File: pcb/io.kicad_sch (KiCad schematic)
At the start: 36 parts, among them J10 Conn_01x02, J2 RJ18, J3 RJ18, J4 Conn_02x05, J5 Conn_01x03, J6 Conn_01x03, J7 Conn_01x02, J8 Conn_01x02, J9 Conn_01x02, Q1 BT148, Q2 BC847, Q3 BC847, U7 6N137, U8 PC817, U9 PC817

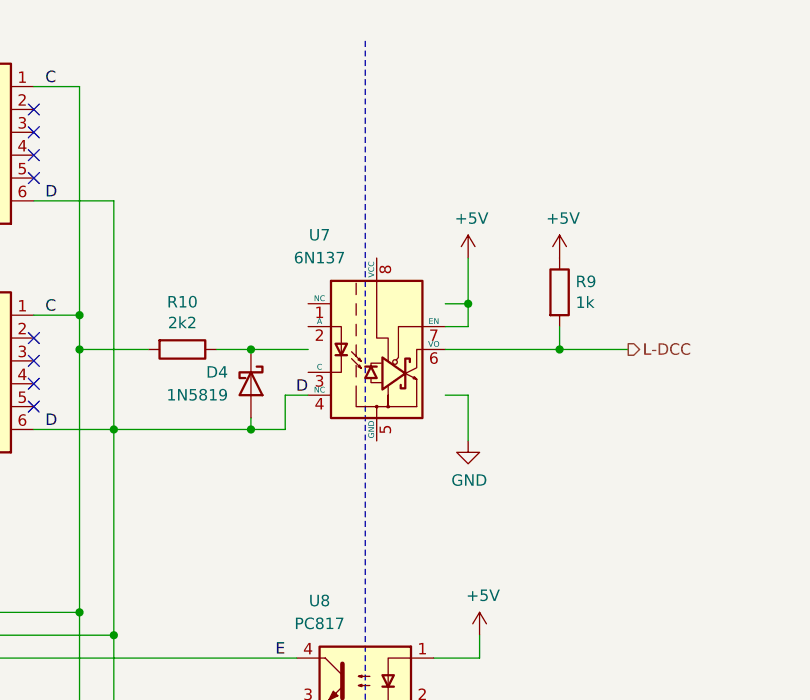
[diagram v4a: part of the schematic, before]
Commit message: Add capacitor to U7, fix new parts.
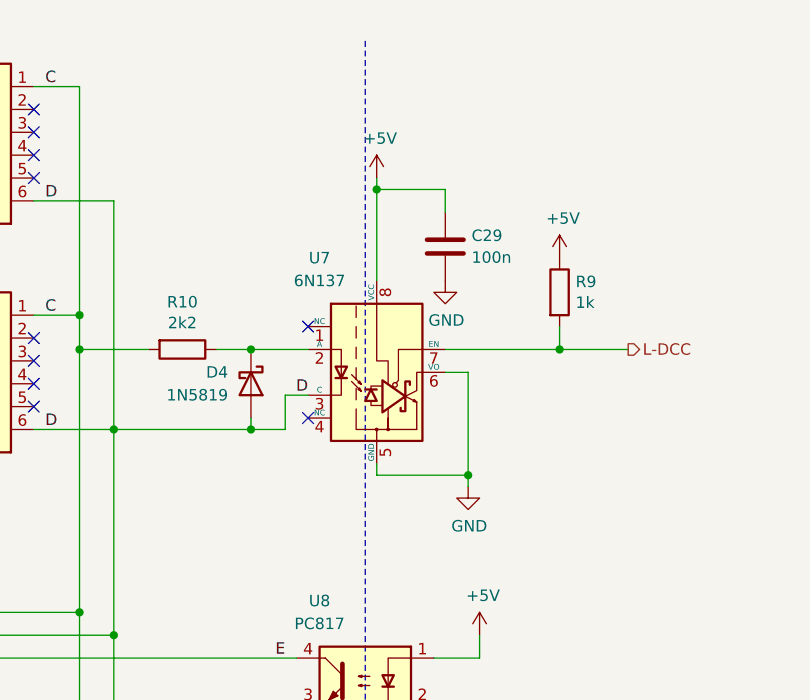
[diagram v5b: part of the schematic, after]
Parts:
- added C29: 100n, Capacitor_SMD:C_0805_2012Metric, symbol Device:C
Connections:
- net +5V: now also U7.8 (VCC), C29.1; no longer U7.7 (EN)
- net D: now also U7.3 (C); no longer U7.4 (NC)
- net GND: now also U7.5 (GND), U7.6 (VO), C29.2
- net L-DCC: now also U7.7 (EN); no longer U7.6 (VO)
- net at U7.2 (A): now also D4.1 (K), R10.1
- no-connect marks 9 -> 11
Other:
- moved on the sheet: U7
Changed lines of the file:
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@@
 	)
 	(junction
+		(at 83.82 35.56)
+		(diameter 0)
+		(color 0 0 0 0)
+	)
+	(junction
 		(at 204.47 55.88)
 		(diameter 0)
@@
 	)
 	(junction
-		(at 93.98 48.26)
+		(at 255.27 123.19)
 		(diameter 0)
 		(color 0 0 0 0)
 	)
 	(junction
-		(at 255.27 123.19)
+		(at 69.85 53.34)
 		(diameter 0)
 		(color 0 0 0 0)
 	)
 	(junction
-		(at 69.85 53.34)
+		(at 214.63 102.87)
 		(diameter 0)
 		(color 0 0 0 0)
 	)
 	(junction
-		(at 214.63 102.87)
+		(at 93.98 67.31)
 		(diameter 0)
 		(color 0 0 0 0)
@@
 	)
 	(no_connect
+		(at 76.2 60.96)
+	)
+	(no_connect
 		(at 45.72 26.67)
 	)
@@
 	)
 	(no_connect
+		(at 76.2 50.8)
+	)
+	(no_connect
 		(at 45.72 54.61)
 	)
@@
 	(wire
 		(pts
+			(xy 83.82 66.04) (xy 83.82 67.31)
+		)
+		(stroke
+			(width 0)
+			(type default)
+		)
+	)
+	(wire
+		(pts
 			(xy 184.15 129.54) (xy 184.15 110.49)
 		)
@@
 		)
 	)
+	(wire
+		(pts
+			(xy 93.98 67.31) (xy 93.98 68.58)
+		)
+		(stroke
+			(width 0)
+			(type default)
+		)
+	)
 	(polyline
 		(pts
@@
 	(wire
 		(pts
-			(xy 91.44 48.26) (xy 93.98 48.26)
-		)
-		(stroke
-			(width 0)
-			(type default)
-		)
-	)
-	(wire
-		(pts
 			(xy 246.38 34.29) (xy 246.38 36.83)
 		)
@@
 	(wire
 		(pts
+			(xy 83.82 67.31) (xy 93.98 67.31)
+		)
+		(stroke
+			(width 0)
+			(type default)
+		)
+	)
+	(wire
+		(pts
 			(xy 34.29 87.63) (xy 40.64 87.63)
 		)
@@
 	(wire
 		(pts
+			(xy 91.44 35.56) (xy 83.82 35.56)
+		)
+		(stroke
+			(width 0)
+			(type default)
+		)
+	)
+	(wire
+		(pts
 			(xy 104.14 53.34) (xy 104.14 50.8)
 		)
@@
 	(wire
 		(pts
-			(xy 91.44 58.42) (xy 93.98 58.42)
-		)
-		(stroke
-			(width 0)
-			(type default)
-		)
-	)
-	(wire
-		(pts
-			(xy 93.98 50.8) (xy 91.44 50.8)
+			(xy 91.44 55.88) (xy 93.98 55.88)
 		)
 		(stroke
@@
 	(wire
 		(pts
+			(xy 83.82 35.56) (xy 83.82 34.29)
+		)
+		(stroke
+			(width 0)
+			(type default)
+		)
+	)
+	(wire
+		(pts
 			(xy 69.85 53.34) (xy 66.04 53.34)
 		)
@@
 	(wire
 		(pts
-			(xy 93.98 48.26) (xy 93.98 50.8)
-		)
-		(stroke
-			(width 0)
-			(type default)
-		)
-	)
-	(wire
-		(pts
 			(xy 105.41 166.37) (xy 102.87 166.37)
 		)
@@
 	(wire
 		(pts
+			(xy 91.44 38.1) (xy 91.44 35.56)
+		)
+		(stroke
+			(width 0)
+			(type default)
+		)
+	)
+	(wire
+		(pts
 			(xy 34.29 82.55) (xy 50.8 82.55)
 		)
@@
 	(wire
 		(pts
-			(xy 93.98 48.26) (xy 93.98 43.18)
+			(xy 83.82 45.72) (xy 83.82 35.56)
 		)
 		(stroke
@@
 	(wire
 		(pts
-			(xy 93.98 58.42) (xy 93.98 63.5)
+			(xy 93.98 55.88) (xy 93.98 67.31)
 		)
 		(stroke
@@
 	(symbol
 		(lib_id "Isolator:6N137")
-		(at 83.82 53.34 0)
+		(at 83.82 55.88 0)
 		(unit 1)
 		(exclude_from_sim no)
@@
 		(dnp no)
 		(property "Reference" "U7"
-			(at 77.47 40.64 0)
+			(at 77.47 43.18 0)
 			(effects
 				(font
@@
 		)
 		(property "Value" "6N137"
-			(at 77.47 43.18 0)
+			(at 77.47 45.72 0)
 			(effects
 				(font
@@
 		)
 		(property "Footprint" "Package_DIP:DIP-8_W7.62mm"
-			(at 83.82 66.04 0)
+			(at 83.82 68.58 0)
 			(effects
 				(font
@@
 		)
 		(property "Datasheet" "https://docs.broadcom.com/docs/AV02-0940EN"
-			(at 62.23 39.37 0)
+			(at 62.23 41.91 0)
 			(effects
 				(font
@@
 		)
 		(property "Description" "Single High Speed LSTTL/TTL Compatible Optocoupler with enable, dV/dt 1000/us, VCM 10, max 7V VCC, DIP-8"
-			(at 83.82 53.34 0)
+			(at 83.82 55.88 0)
 			(effects
 				(font
@@
 	(symbol
 		(lib_id "power:+5V")
-		(at 93.98 43.18 0)
+		(at 83.82 34.29 0)
 		(unit 1)
 		(exclude_from_sim no)
@@
 		(dnp no)
 		(property "Reference" "#PWR0123"
-			(at 93.98 46.99 0)
+			(at 83.82 38.1 0)
 			(effects
 				(font
@@
 		)
 		(property "Value" "+5V"
-			(at 94.361 38.7858 0)
+			(at 84.201 29.8958 0)
 			(effects
 				(font
@@
 		)
 		(property "Footprint" ""
-			(at 93.98 43.18 0)
+			(at 83.82 34.29 0)
 			(effects
 				(font
@@
 		)
 		(property "Datasheet" ""
-			(at 93.98 43.18 0)
+			(at 83.82 34.29 0)
 			(effects
 				(font
@@
 		)
 		(property "Description" "Power symbol creates a global label with name \"+5V\""
-			(at 93.98 43.18 0)
+			(at 83.82 34.29 0)
 			(effects
 				(font
@@
 	(symbol
 		(lib_id "power:GND")
-		(at 93.98 63.5 0)
+		(at 93.98 68.58 0)
 		(unit 1)
 		(exclude_from_sim no)
@@
 		(dnp no)
 		(property "Reference" "#PWR0124"
-			(at 93.98 69.85 0)
+			(at 93.98 74.93 0)
 			(effects
 				(font
@@
 		)
 		(property "Value" "GND"
-			(at 94.107 67.8942 0)
+			(at 94.107 72.9742 0)
 			(effects
 				(font
@@
 		)
 		(property "Footprint" ""
-			(at 93.98 63.5 0)
+			(at 93.98 68.58 0)
 			(effects
 				(font
@@
 		)
 		(property "Datasheet" ""
-			(at 93.98 63.5 0)
+			(at 93.98 68.58 0)
 			(effects
 				(font
@@
 		)
 		(property "Description" "Power symbol creates a global label with name \"GND\" , ground"
-			(at 93.98 63.5 0)
+			(at 93.98 68.58 0)
 			(effects
 				(font
@@
 					(unit 1)
 				)
+			)
+		)
+	)
+	(symbol
+		(lib_id "power:GND")
+		(at 91.44 45.72 0)
+		(unit 1)
+		(exclude_from_sim no)
+		(in_bom yes)
+		(on_board yes)
+		(dnp no)
+		(property "Reference" "#PWR011"
+			(at 91.44 52.07 0)
+			(effects
+				(font
+					(size 1.27 1.27)
+				)
+				(hide yes)
+			)
+		)
+		(property "Value" "GND"
+			(at 91.567 50.1142 0)
+			(effects
+				(font
+					(size 1.27 1.27)
+				)
+			)
+		)
+		(property "Footprint" ""
+			(at 91.44 45.72 0)
+			(effects
+				(font
+					(size 1.27 1.27)
+				)
+				(hide yes)
+			)
+		)
+		(property "Datasheet" ""
+			(at 91.44 45.72 0)
+			(effects
+				(font
+					(size 1.27 1.27)
+				)
+				(hide yes)
+			)
+		)
+		(property "Description" "Power symbol creates a global label with name \"GND\" , ground"
+			(at 91.44 45.72 0)
+			(effects
+				(font
+					(size 1.27 1.27)
+				)
+				(hide yes)
+			)
+		)
+		(pin "1"
+		)
+		(instances
+			(project "hb22"
+				(path "/99e6b8eb-b08e-4d42-84dd-8b7f6765b7b7/00000000-0000-0000-0000-000061edd3fc"
+					(reference "#PWR011")
+					(unit 1)
+				)
+			)
+		)
+	)
+	(symbol
+		(lib_id "Device:C")
+		(at 91.44 41.91 0)
+		(unit 1)
+		(exclude_from_sim no)
+		(in_bom yes)
+		(on_board yes)
+		(dnp no)
+		(fields_autoplaced yes)
+		(property "Reference" "C29"
+			(at 94.361 40.6978 0)
+			(effects
+				(font
+					(size 1.27 1.27)
+				)
+				(justify left)
+			)
+		)
+		(property "Value" "100n"
+			(at 94.361 43.1221 0)
+			(effects
+				(font
+					(size 1.27 1.27)
+				)
+				(justify left)
+			)
+		)
+		(property "Footprint" "Capacitor_SMD:C_0805_2012Metric"
+			(at 92.4052 45.72 0)
+			(effects
+				(font
+					(size 1.27 1.27)
+				)
+				(hide yes)
+			)
+		)
+		(property "Datasheet" "~"
+			(at 91.44 41.91 0)
+			(effects
+				(font
+					(size 1.27 1.27)
+				)
+				(hide yes)
+			)
+		)
+		(property "Description" "Unpolarized capacitor"
+			(at 91.44 41.91 0)
+			(effects
+				(font
+					(size 1.27 1.27)
+				)
+				(hide yes)
+			)
+		)
+		(pin "1"
+		)
+		(pin "2"
+		)
+		(instances
+			(project ""
+				(path "/99e6b8eb-b08e-4d42-84dd-8b7f6765b7b7/00000000-0000-0000-0000-000061edd3fc"
+					(reference "C29")
+					(unit 1)
+				)

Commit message: Use normal SMD footprints, avoid handsolder.
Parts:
- C6, C7: footprint Capacitor_SMD:C_0805_2012Metric_Pad1.18x1.45mm_HandSolder -> Capacitor_SMD:C_0805_2012Metric
- D8: footprint Diode_SMD:D_SMA_Handsoldering -> Diode_SMD:D_SMA
- F1: footprint Fuse:Fuse_1206_3216Metric_Pad1.42x1.75mm_HandSolder -> Fuse:Fuse_1206_3216Metric
- R10, R11, R12, R13, R14, R15, R16, R5, R8, R9: footprint Resistor_SMD:R_0805_2012Metric_Pad1.20x1.40mm_HandSolder -> Resistor_SMD:R_0805_2012Metric
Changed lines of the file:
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@@
 			)
 		)
-		(property "Footprint" "Diode_SMD:D_SMA_Handsoldering"
+		(property "Footprint" "Diode_SMD:D_SMA"
 			(at 224.79 106.68 0)
 			(effects
@@
 			)
 		)
-		(property "Footprint" "Fuse:Fuse_1206_3216Metric_Pad1.42x1.75mm_HandSolder"
+		(property "Footprint" "Fuse:Fuse_1206_3216Metric"
 			(at 247.65 35.56 0)
 			(effects
@@
 			)
 		)
-		(property "Footprint" "Resistor_SMD:R_0805_2012Metric_Pad1.20x1.40mm_HandSolder"
+		(property "Footprint" "Resistor_SMD:R_0805_2012Metric"
 			(at 249.682 40.64 90)
 			(effects
@@
 			)
 		)
-		(property "Footprint" "Resistor_SMD:R_0805_2012Metric_Pad1.20x1.40mm_HandSolder"
+		(property "Footprint" "Resistor_SMD:R_0805_2012Metric"
 			(at 202.692 40.64 90)
 			(effects
@@
 			)
 		)
-		(property "Footprint" "Resistor_SMD:R_0805_2012Metric_Pad1.20x1.40mm_HandSolder"
+		(property "Footprint" "Resistor_SMD:R_0805_2012Metric"
 			(at 205.74 56.642 90)
 			(effects
@@
 			)
 		)
-		(property "Footprint" "Resistor_SMD:R_0805_2012Metric_Pad1.20x1.40mm_HandSolder"
+		(property "Footprint" "Resistor_SMD:R_0805_2012Metric"
 			(at 93.472 100.33 90)
 			(effects
@@
 			)
 		)
-		(property "Footprint" "Resistor_SMD:R_0805_2012Metric_Pad1.20x1.40mm_HandSolder"
+		(property "Footprint" "Resistor_SMD:R_0805_2012Metric"
 			(at 109.22 116.078 90)
 			(effects
@@
 			)
 		)
-		(property "Footprint" "Resistor_SMD:R_0805_2012Metric_Pad1.20x1.40mm_HandSolder"
+		(property "Footprint" "Resistor_SMD:R_0805_2012Metric"
 			(at 62.23 51.562 90)
 			(effects
@@
 			)
 		)
-		(property "Footprint" "Resistor_SMD:R_0805_2012Metric_Pad1.20x1.40mm_HandSolder"
+		(property "Footprint" "Resistor_SMD:R_0805_2012Metric"
 			(at 102.362 46.99 90)
 			(effects
@@
 			)
 		)
-		(property "Footprint" "Resistor_SMD:R_0805_2012Metric_Pad1.20x1.40mm_HandSolder"
+		(property "Footprint" "Resistor_SMD:R_0805_2012Metric"
 			(at 93.472 152.4 90)
 			(effects
@@
 			)
 		)
-		(property "Footprint" "Resistor_SMD:R_0805_2012Metric_Pad1.20x1.40mm_HandSolder"
+		(property "Footprint" "Resistor_SMD:R_0805_2012Metric"
 			(at 109.22 168.148 90)
 			(effects
@@
 			)
 		)
-		(property "Footprint" "Capacitor_SMD:C_0805_2012Metric_Pad1.18x1.45mm_HandSolder"
+		(property "Footprint" "Capacitor_SMD:C_0805_2012Metric"
 			(at 194.0052 115.57 0)
 			(effects
@@
 			)
 		)
-		(property "Footprint" "Resistor_SMD:R_0805_2012Metric_Pad1.20x1.40mm_HandSolder"
+		(property "Footprint" "Resistor_SMD:R_0805_2012Metric"
 			(at 201.422 119.38 90)
 			(effects
@@
 			)
 		)
-		(property "Footprint" "Capacitor_SMD:C_0805_2012Metric_Pad1.18x1.45mm_HandSolder"
+		(property "Footprint" "Capacitor_SMD:C_0805_2012Metric"
 			(at 215.5952 123.19 0)
 			(effects
